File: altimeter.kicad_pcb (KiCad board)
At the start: 4 copper layers, 45 x 24 mm, 75 parts, among them J201 Conn_01x10, J202 Conn_ARM_JTAG_SWD_10, J203 Conn_02x03_Counter_Clockwise, J204 USB_B_Micro, J205 Conn_01x04, Q1 BC847BDW1, Q101 DMG2301L, Q102 DMG2301L, Q301 BC847BDW1, Q401 BC847BDW1, Q501 BC847BDW1, U1 LMV331, U101 STM32F302CCTx, U102 S25L512S, U103 AIS2120SXTR, U104 MIC5219-3.3YM5, U105 LF50_TO252, U107 MS5611-01BA, U301 SI7232DN, U501 SI7232DN, Y1 Crystal_GND24

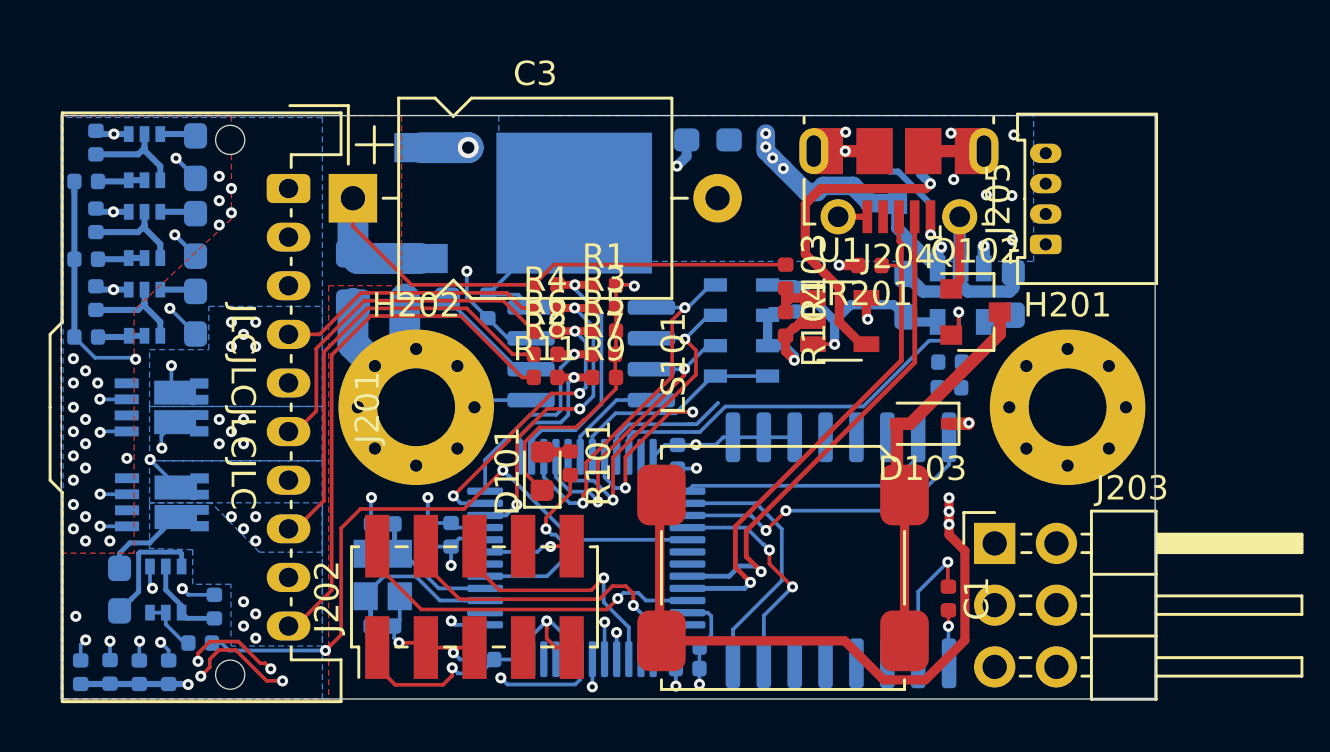
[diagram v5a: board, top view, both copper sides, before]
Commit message: nearly finished with lacout. Added logo
Signed-off-by: Thomas Schmid <tom@binary-kitchen.de>
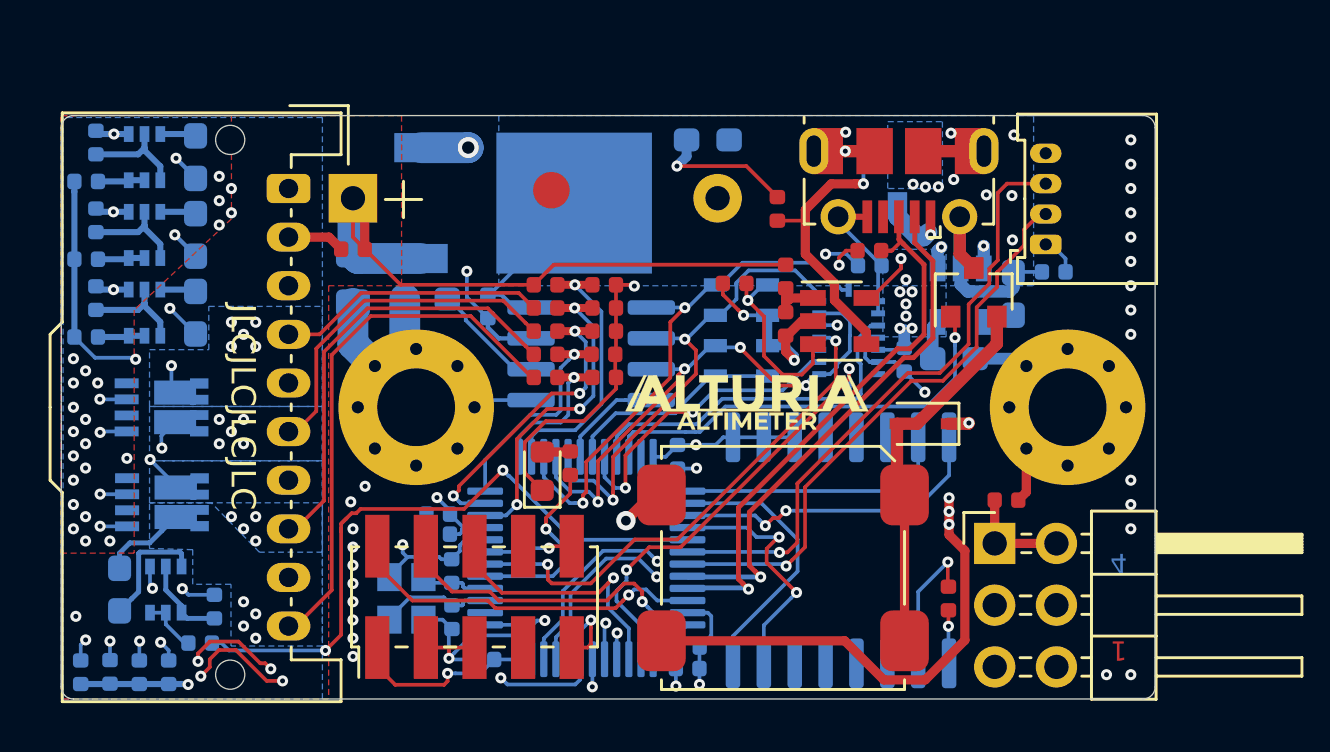
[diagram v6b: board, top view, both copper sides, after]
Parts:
- added C201: C, Capacitor_SMD:C_0402_1005Metric, F.Cu at (150.0, 102.5)
- added C202: C, Capacitor_SMD:C_0402_1005Metric, F.Cu at (176.9, 112.8)
- added C203: C, Capacitor_SMD:C_0402_1005Metric, B.Cu at (178.8, 103.4)
- added R102: 2.7k, Resistor_SMD:R_0402_1005Metric, F.Cu at (167.5, 100.8)
- added REF**: Fiducial_1.5mm_Mask3mm, Fiducial:Fiducial_1.5mm_Mask3mm, F.Cu at (158.2, 100.1)
- added Ref**: alturia_logo, altimeter:alturia_logo, F.Cu at (166.2, 108.8)
- added U106: BMI088, altimeter:BMI088, B.Cu at (170.4, 106.1)
- C105: value C_Small -> 470p
- C106: moved to F.Cu
- C108: value C_Small -> 4.7u
- C111, C112, C113, C114, C115, C116: value C_Small -> 100n
- Q1, Q301, Q401, Q501: value BC847BDW1 -> BC848CDW1T1G
- Q102: value DMG2301L -> NTR4003NT1G
- U102: value S25L512S -> S25FL512SAGMFIR11
- moved C109 6.00 mm to (171.3, 103.2), turned to 180 degrees
- moved C102 3.43 mm to (154.1, 115.7), turned to 90 degrees
- moved C108 3.26 mm to (174.7, 107.0), turned to 0 degrees
- moved C101 2.88 mm to (154.1, 117.6), turned to 270 degrees
- moved C106 2.68 mm to (165.7, 103.9), turned to 0 degrees
- moved C110 1.89 mm to (172.7, 107.0), turned to 90 degrees
- moved Y1 1.37 mm to (152.2, 116.9)
- moved C114 1.00 mm to (153.5, 113.4), turned to 180 degrees
- moved Q102 0.82 mm to (175.5, 104.3), turned to 90 degrees
- moved R201 0.61 mm to (171.2, 102.6)
- moved C112 0.42 mm to (153.5, 114.2), turned to 180 degrees
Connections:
- J203 pad 1: Net-(J203-Pad1) -> +5V
- J203 pad 2: Net-(J203-Pad2) -> +5V
- J203 pad 3: Net-(J203-Pad3) -> PWM1
- J203 pad 4: Net-(J203-Pad4) -> PWM2
- J203 pad 5: Net-(J203-Pad5) -> GND
- J203 pad 6: Net-(J203-Pad6) -> GND
- J205 pad 1: Net-(J205-Pad1) -> +3V3
- J205 pad 2: Net-(J205-Pad2) -> UART1_RX
- J205 pad 3: Net-(J205-Pad3) -> UART1_TX
- J205 pad 4: Net-(J205-Pad4) -> GND
- Q101 pad 1: VBUS -> Net-(Q101-Pad1)
- Q101 pad 2: Net-(Q101-Pad2) -> +5V
- Q101 pad 3: +5V -> VBUS
- Q102 pad 1: GND -> SUMMER
- Q102 pad 2: SUMMER -> Net-(D103-Pad2)
- Q102 pad 3: Net-(D103-Pad2) -> GND
- U1 pad 4: Net-(Q101-Pad2) -> Net-(Q101-Pad1)
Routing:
- net PWM2: track 0.00 -> 26.1 mm, vias 0 -> 1
- net UART1_TX: track 0.00 -> 25.4 mm, vias 0 -> 1
- net GND: track 99.7 -> 123.8 mm, vias 47 -> 71
- net UART1_RX: track 0.00 -> 23.9 mm, vias 0 -> 1
- net PWM1: track 0.00 -> 22.1 mm, vias 0 -> 1
- net INT2: track 0.00 -> 21.0 mm, vias 0 -> 2
- net INT1: track 0.00 -> 17.8 mm, vias 0 -> 2
- net Net-(Q101-Pad2): track 13.8 -> 0.00 mm, vias 1 -> 0
- net Net-(Q101-Pad1): track 0.00 -> 12.5 mm, vias 0 -> 1
- net +3V3: track 40.0 -> 50.5 mm, vias 9 -> 16
- net SPI1_MISO: track 13.0 -> 22.6 mm, vias 2 -> 4
- net +5V: track 45.6 -> 55.0 mm
- net IMU_ACC_CS: track 5.58 -> 15.0 mm
- net SPI1_SCK: track 15.7 -> 22.0 mm
- net SPI1_MOSI: track 14.3 -> 20.5 mm
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- added copper zone on B.Cu, net +3V3
- added copper zone on In1.Cu, net +3V3
- added copper zone on B.Cu, net +5V
- added copper zone on In1.Cu, net +5V
- added copper zone on In2.Cu, net PYRO0_HIGH
- added copper zone on In1.Cu, net PYRO0_LOW
- added copper zone on In1.Cu, net PYRO1_LOW
- added copper zone on In1.Cu, net PYRO2_LOW
- added copper zone on In1.Cu, net PYRO3_LOW
- removed copper zone on In2.Cu, net +3V3
- removed copper zone on In2.Cu, net +5V
- removed copper zone on In1.Cu, net PYRO0_HIGH
- removed copper zone on In2.Cu, net PYRO0_LOW
- removed copper zone on In2.Cu, net PYRO1_LOW
- removed copper zone on In2.Cu, net PYRO2_LOW
- removed copper zone on In2.Cu, net PYRO3_LOW
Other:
- outline, holes or cut-outs redrawn
- rule solder_mask_min_width: 0.127 -> 0.1
- rule trace_min: 0.127 -> 0.152
- board text added: "1"
- board text added: "2"
- board text added: "3"
- board text added: "4"

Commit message: completed layout
Signed-off-by: Thomas Schmid <tom@binary-kitchen.de>
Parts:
- removed REF**: Fiducial_1.5mm_Mask3mm, Fiducial:Fiducial_1.5mm_Mask3mm
- added Q103: SiSS05DN, Package_SO:Vishay_PowerPAK_1212-8_Single, F.Cu at (153.4, 99.4)
- added Ref**: up_arrow, altimeter:up_arrow, F.Cu at (158.3, 109.2)
- added Ref**: alturia_license, altimeter:alturia_license, B.Cu at (180.9, 100.3)
- added U201: USBLC6-2SC6, Package_TO_SOT_SMD:SOT-666, F.Cu at (173.2, 103.6)
- C201: moved to B.Cu
- moved C201 5.13 mm to (146.6, 98.7)
- moved C109 0.81 mm to (170.9, 102.4)
- moved Q102 0.59 mm to (175.8, 104.8)
- moved Ref** 0.44 mm to (166.5, 109.1)
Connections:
- C201 pad 1: PYRO0_HIGH -> +BATT
- J201 pad 1: PYRO0_HIGH -> +BATT
- J204 pad 2: USB_D_N -> Net-(J204-Pad2)
- J204 pad 3: USB_D_P -> Net-(J204-Pad3)
- R201 pad 1: USB_D_P -> Net-(J204-Pad3)
- U101 pad 2: Net-(U101-Pad2) -> FLASH_HOLD
- U102 pad 1: +3V3 -> FLASH_HOLD
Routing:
- net FLASH_HOLD: track 0.00 -> 14.2 mm, vias 0 -> 2
- net PYRO0_HIGH: track 28.0 -> 36.6 mm
- net +5V: track 55.0 -> 61.1 mm, vias 13 -> 14
- net USB_D_P: track 23.3 -> 18.0 mm
- net USB_D_N: track 21.7 -> 18.1 mm
- net VBUS: track 2.99 -> 6.61 mm
- net GND: track 123.8 -> 127.3 mm, vias 71 -> 67
- net Net-(J204-Pad3): track 0.00 -> 2.66 mm
- net +3V3: track 50.5 -> 53.1 mm, vias 16 -> 13
- net Net-(J204-Pad2): track 0.00 -> 2.07 mm
- net +BATT: track 0.00 -> 1.61 mm, vias 0 -> 18
- net SUMMER: track 17.9 -> 19.3 mm
- net PYRO1_SENSE: track 12.8 -> 13.4 mm
- net PYRO1_LOW: track 28.6 -> 28.0 mm
- net PYRO3_LOW: track 27.2 -> 26.6 mm
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- added copper zone on B.Cu, net +BATT
- added copper zone on F.Cu, net +BATT
- added copper zone on In1.Cu, net +BATT
- added copper zone on In2.Cu, net +BATT

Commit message: minor updates
Signed-off-by: Thomas Schmid <tom@lfence.de>
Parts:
- removed the Ref** at (180.9, 100.3)
- added R105: 100k, Resistor_SMD:R_0402_1005Metric, F.Cu at (157.6, 100.8)
- C201, C202, C203: value C -> 100n
- Q103: value SiSS05DN -> SISS05dn
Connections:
- Q103 pad 4: GND -> Net-(D102-Pad1)
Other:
- board text added: "CC-BY-NC-SA 4.0"
